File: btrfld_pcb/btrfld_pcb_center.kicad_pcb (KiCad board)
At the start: 2 copper layers, 82 x 64.8 mm, 39 parts

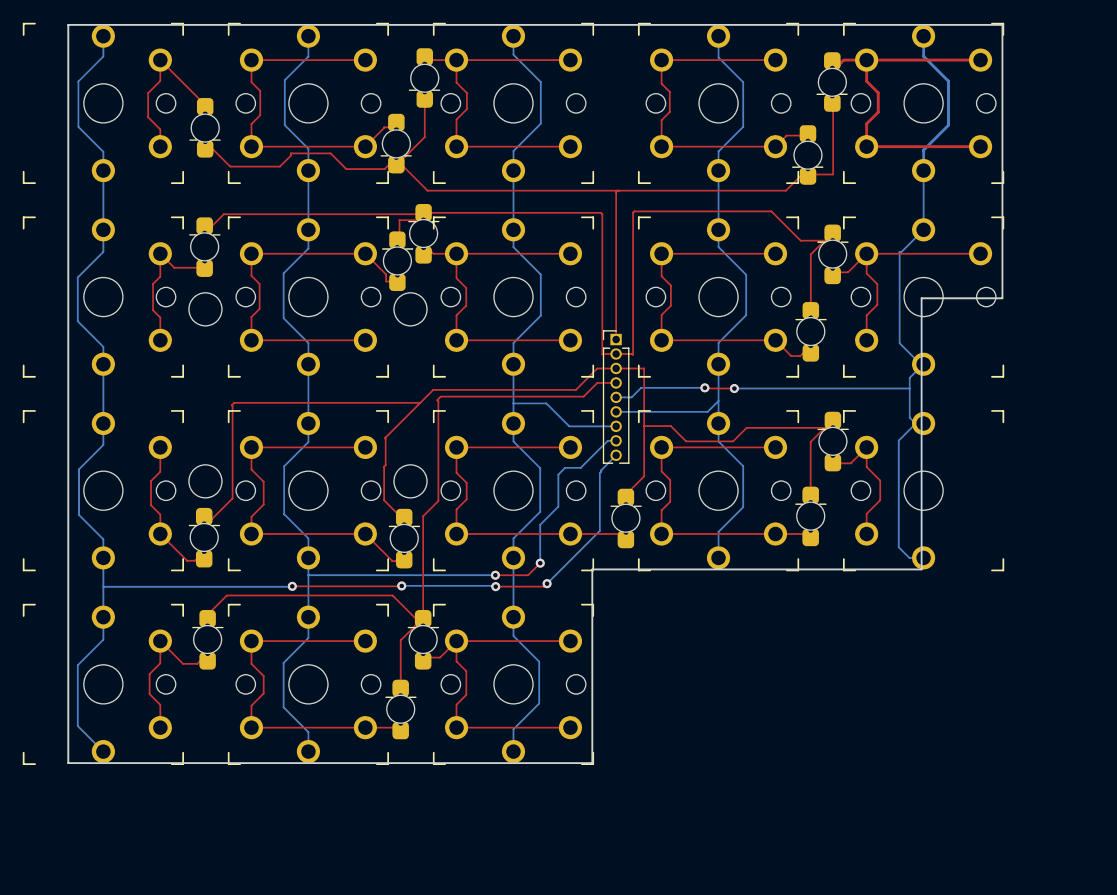
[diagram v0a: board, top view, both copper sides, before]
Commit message: add pcb for center board
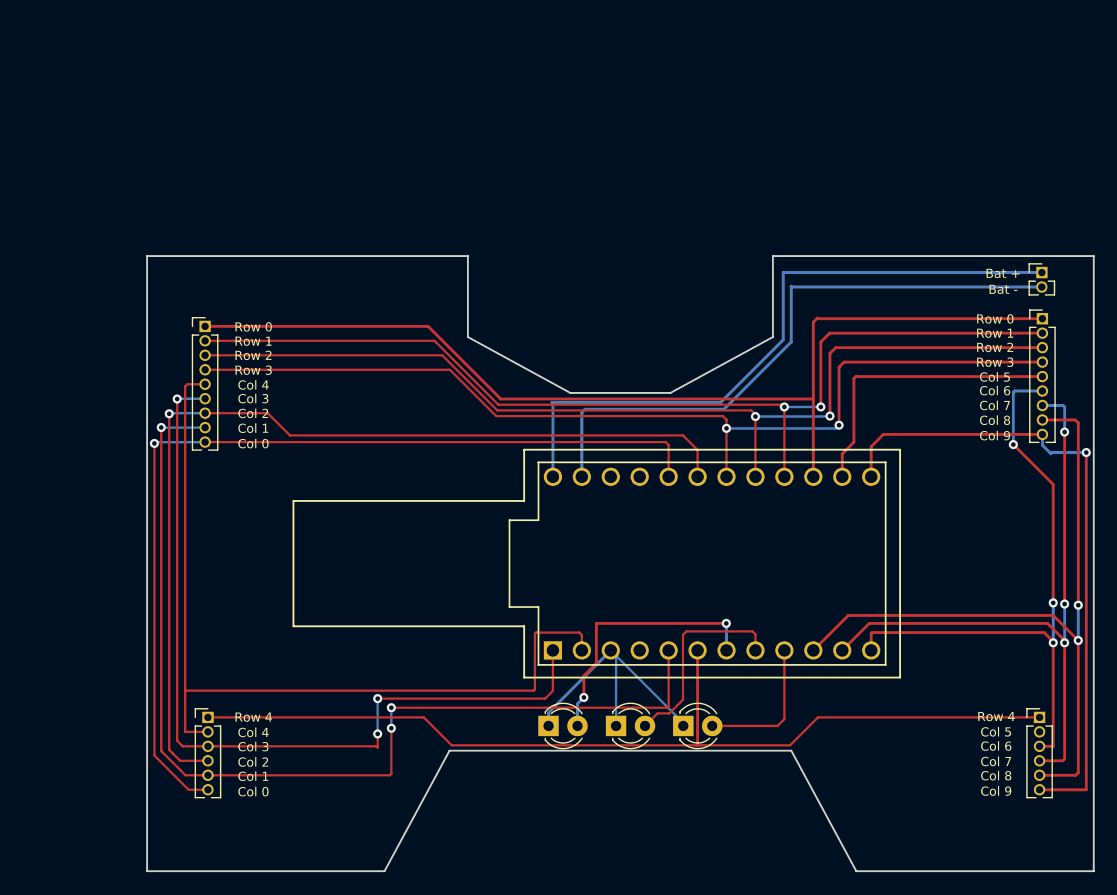
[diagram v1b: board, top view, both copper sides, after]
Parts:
- removed the REF** at (144.3, 83.1)
- removed the REF** at (125.0, 68.9)
- removed the REF** at (171.3, 62.4)
- removed the REF** at (125.4, 112.5)
- removed the REF** at (153.3, 79.3)
- removed the REF** at (163.3, 63.5)
- removed the REF** at (163.4, 89.0)
- removed the REF** at (153.3, 96.3)
- removed the REF** at (108.5, 106.4)
- removed the REF** at (127.4, 106.4)
- removed the REF** at (161.4, 95.6)
- removed the REF** at (108.3, 67.5)
- removed the REF** at (127.4, 70.8)
- removed the REF** at (108.2, 71.9)
- removed the REF** at (163.3, 72.6)
- removed the REF** at (171.3, 96.3)
- removed the REF** at (135.3, 96.3)
- removed the REF** at (99.3, 79.3)
- removed the REF** at (117.3, 79.3)
- removed the REF** at (125.1, 73.2)
- removed the REF** at (153.3, 62.4)
- removed the REF** at (135.3, 62.4)
- removed the REF** at (117.3, 96.3)
- removed the REF** at (161.2, 69.9)
- removed the REF** at (117.3, 62.4)
- removed the REF** at (99.3, 62.4)
- removed the REF** at (135.3, 79.3)
- removed the REF** at (117.3, 113.3)
- removed the REF** at (171.3, 79.3)
- removed the REF** at (145.2, 95.7)
- removed the REF** at (135.3, 113.3)
- removed the REF** at (127.5, 63.2)
- removed the REF** at (161.4, 79.4)
- removed the REF** at (99.3, 113.3)
- removed the REF** at (99.3, 96.3)
- removed the REF** at (108.3, 95.5)
- removed the REF** at (108.2, 97.4)
- removed the REF** at (126.3, 95.5)
- removed the REF** at (125.7, 97.5)
- added REF**: PinHeader_1x09_P1.27mm_Vertical, Connector_PinHeader_1.27mm:PinHeader_1x09_P1.27mm_Vertical, F.Cu at (181.8, 81.2)
- added REF**: ProMicro, SW_KEYBOARD:ProMicro, F.Cu at (152.8, 102.8)
- added REF**: LED_D3.0mm, LED_THT:LED_D3.0mm, F.Cu at (138.4, 117.0)
- added REF**: PinHeader_1x06_P1.27mm_Vertical, Connector_PinHeader_1.27mm:PinHeader_1x06_P1.27mm_Vertical, F.Cu at (181.5, 116.2)
- added REF**: PinHeader_1x06_P1.27mm_Vertical, Connector_PinHeader_1.27mm:PinHeader_1x06_P1.27mm_Vertical, F.Cu at (108.5, 116.2)
- added REF**: PinHeader_1x02_P1.27mm_Vertical, Connector_PinHeader_1.27mm:PinHeader_1x02_P1.27mm_Vertical, F.Cu at (181.7, 77.2)
- added REF**: LED_D3.0mm, LED_THT:LED_D3.0mm, F.Cu at (150.2, 117.0)
- added REF**: LED_D3.0mm, LED_THT:LED_D3.0mm, F.Cu at (144.3, 117.0)
- added REF**: PinHeader_1x09_P1.27mm_Vertical, Connector_PinHeader_1.27mm:PinHeader_1x09_P1.27mm_Vertical, F.Cu at (108.2, 81.9)
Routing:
- net (no net): track 1272.7 -> 1283.0 mm, vias 8 -> 25
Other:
- board size 82 x 64.8 mm -> 83.1 x 54 mm
- board text added: "Bat +"
- board text added: "Bat -"
- board text added: "Col 0"
- board text added: "Col 1"
- board text added: "Col 2"
- board text added: "Col 3"
- board text added: "Col 4"
- board text added: "Col 5"
- board text added: "Col 6"
- board text added: "Col 7"
- board text added: "Col 8"
- board text added: "Col 9"
- board text added: "Row 0"
- board text added: "Row 1"
- board text added: "Row 2"
- board text added: "Row 3"
- board text added: "Row 4"

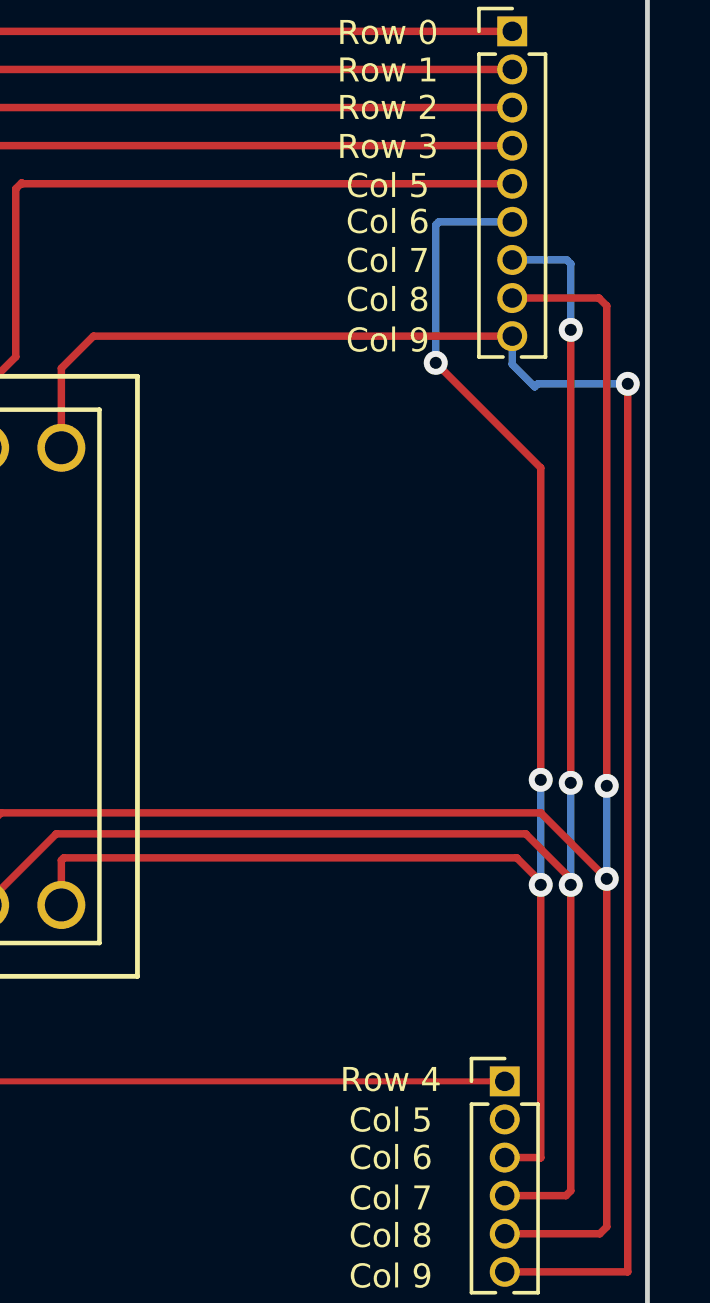
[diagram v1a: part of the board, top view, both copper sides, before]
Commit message: correct column 5 trace on center pcb
add center pcb to cad
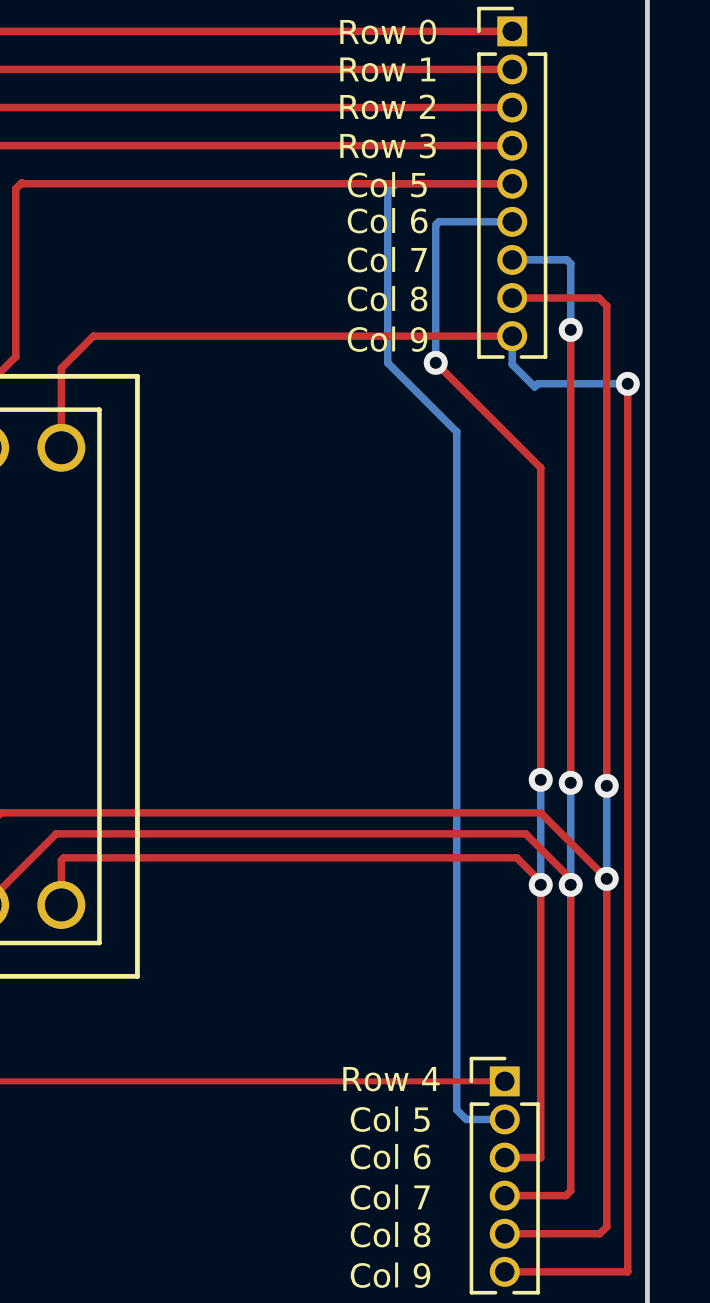
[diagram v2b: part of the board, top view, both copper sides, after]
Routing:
- net (no net): track 1283.0 -> 1320.6 mm
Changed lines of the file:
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@@
   (via (at 154 108) (size 0.8) (drill 0.4) (layers "F.Cu" "B.Cu") (free) (net 0))
   (via (at 162.3 89) (size 0.8) (drill 0.4) (layers "F.Cu" "B.Cu") (net 0))
+  (segment (start 179.9 94.6) (end 177.6 92.3) (width 0.25) (layer "B.Cu") (net 0))
   (segment (start 163.06 89.84) (end 163.1 89.8) (width 0.2) (layer "B.Cu") (net 0))
   (segment (start 141.32 89.48) (end 141.32 95.13) (width 0.25) (layer "B.Cu") (net 0))
@@
   (segment (start 138.4 115.83) (end 143.86 110.37) (width 0.25) (layer "B.Cu") (net 0))
   (segment (start 140.94 115.06) (end 141.5 114.5) (width 0.25) (layer "B.Cu") (net 0))
+  (segment (start 179.9 117.2) (end 179.9 94.6) (width 0.25) (layer "B.Cu") (net 0))
   (segment (start 105.1 89.6) (end 105.155 89.545) (width 0.2) (layer "B.Cu") (net 0))
   (segment (start 144.325 110.835) (end 143.86 110.37) (width 0.2) (layer "B.Cu") (net 0))
@@
   (segment (start 159.7 83.3) (end 153.8 89.2) (width 0.25) (layer "B.Cu") (net 0))
   (segment (start 153.5 88.6) (end 138.7 88.6) (width 0.25) (layer "B.Cu") (net 0))
+  (segment (start 177.6 86.6) (end 177.87 86.33) (width 0.25) (layer "B.Cu") (net 0))
   (segment (start 150.225 116.735) (end 143.86 110.37) (width 0.2) (layer "B.Cu") (net 0))
   (segment (start 182.6 93) (end 182.5 93.1) (width 0.25) (layer "B.Cu") (net 0))
@@
   (segment (start 124.6 117.2) (end 124.6 115.4) (width 0.2) (layer "B.Cu") (net 0))
   (segment (start 123.4 117.7) (end 123.4 114.6) (width 0.2) (layer "B.Cu") (net 0))
+  (segment (start 177.6 92.3) (end 177.6 86.6) (width 0.25) (layer "B.Cu") (net 0))
   (segment (start 105.8 88.3) (end 105.825 88.275) (width 0.2) (layer "B.Cu") (net 0))
   (segment (start 159 83.1) (end 153.5 88.6) (width 0.25) (layer "B.Cu") (net 0))
+  (segment (start 181.5 117.52) (end 180.22 117.52) (width 0.25) (layer "B.Cu") (net 0))
   (segment (start 179.3 87.6) (end 181.75 87.6) (width 0.25) (layer "B.Cu") (net 0))
   (segment (start 138.4 117) (end 138.4 115.83) (width 0.25) (layer "B.Cu") (net 0))
@@
   (segment (start 182.7 109.7) (end 182.7 106.2) (width 0.25) (layer "B.Cu") (net 0))
   (segment (start 141.6 89.2) (end 141.32 89.48) (width 0.25) (layer "B.Cu") (net 0))
+  (segment (start 180.22 117.52) (end 179.9 117.2) (width 0.25) (layer "B.Cu") (net 0))
   (segment (start 183.57 88.87) (end 181.75 88.87) (width 0.25) (layer "B.Cu") (net 0))
   (segment (start 104.415 90.815) (end 108.25 90.815) (width 0.2) (layer "B.Cu") (net 0))
   (segment (start 150.225 117) (end 150.225 116.735) (width 0.2) (layer "B.Cu") (net 0))
+  (segment (start 177.87 86.33) (end 181.75 86.33) (width 0.25) (layer "B.Cu") (net 0))
   (segment (start 159.77 78.47) (end 159.7 78.4) (width 0.25) (layer "B.Cu") (net 0))
   (segment (start 105.825 88.275) (end 108.25 88.275) (width 0.2) (layer "B.Cu") (net 0))
